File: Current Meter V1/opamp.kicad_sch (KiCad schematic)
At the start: 14 parts, among them U503 MCP6002-xSN

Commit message: microcontroller update
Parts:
- removed C506, C507: 100nF, symbol Device:C
- removed D501: BAT54A, Package_TO_SOT_SMD:SOT-23, symbol Diode:BAT54A
- removed D502: PRTR5V0U2X, Package_TO_SOT_SMD:SOT-143, symbol Power_Protection:PRTR5V0U2X
- removed R501, R503, R504, R505: 10k Ohms, symbol Device:R_US
- removed R502: 4.7k Ohms, symbol Device:R_US
- removed R506: 20k Ohms, symbol Device:R_US
- removed R507: 3.3K Ohms, symbol Device:R_US
- removed R508: 4.7K Ohms, symbol Device:R_US
- removed TP501: SMD Test Point, TestPoint:TestPoint_Keystone_5019_Miniature, symbol bfr_utilities:SMD_Test_Point
- removed U503: MCP6002-xSN, symbol Amplifier_Operational:MCP6002-xSN
- added C201, C202, C203: 100nF, symbol Device:C
- added D201, D203: BAT54A, Package_TO_SOT_SMD:SOT-23, symbol Diode:BAT54A
- added D202, D204: PRTR5V0U2X, Package_TO_SOT_SMD:SOT-143, symbol Power_Protection:PRTR5V0U2X
- added R201: 1.2k Ohms, symbol Device:R_US
- added R202, R203: 10k Ohms, symbol Device:R_US
- added R204, R207: 8.2K Ohms, symbol Device:R_US
- added R205: 24k Ohms, symbol Device:R_US
- added R206: 20k Ohms, symbol Device:R_US
- added R208: 22K Ohms, symbol Device:R_US
- added TP201, TP202: SMD Test Point, TestPoint:TestPoint_Keystone_5019_Miniature, symbol bfr_utilities:SMD_Test_Point
- added U201, U202: MCP6002-xSN, symbol Amplifier_Operational:MCP6002-xSN
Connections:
- net +3V3: now also D202.4 (VCC), D204.4 (VCC)
- net +5V: now also C202.1, D201.1, D203.1, R203.1, U201.8 (V+)
- net GND: now also C201.2, C202.2, C203.2, D202.1 (GND), D204.1 (GND), R201.2, R204.1, R208.2, U201.4 (V-), U201.5 (+)
- new net: R205.2, R206.1, U201.2 (-)
- new net: R207.1, TP202.1, U202.1, U202.2 (-)
- new net: R202.2, R205.1
- new net: U201.6 (-), U201.7
- new net 0.54V: C201.1, R201.1, R202.1, R203.2
- new net ADC: D202.2 (I/O1), R206.2, TP201.1, U201.1
- new net Sensor: D201.3, D203.3, R204.2, U201.3 (+), U202.3 (+)
- new net curr_sig: C203.1, D204.2 (I/O1), R207.2, R208.1
- no-connect marks 1 -> 4

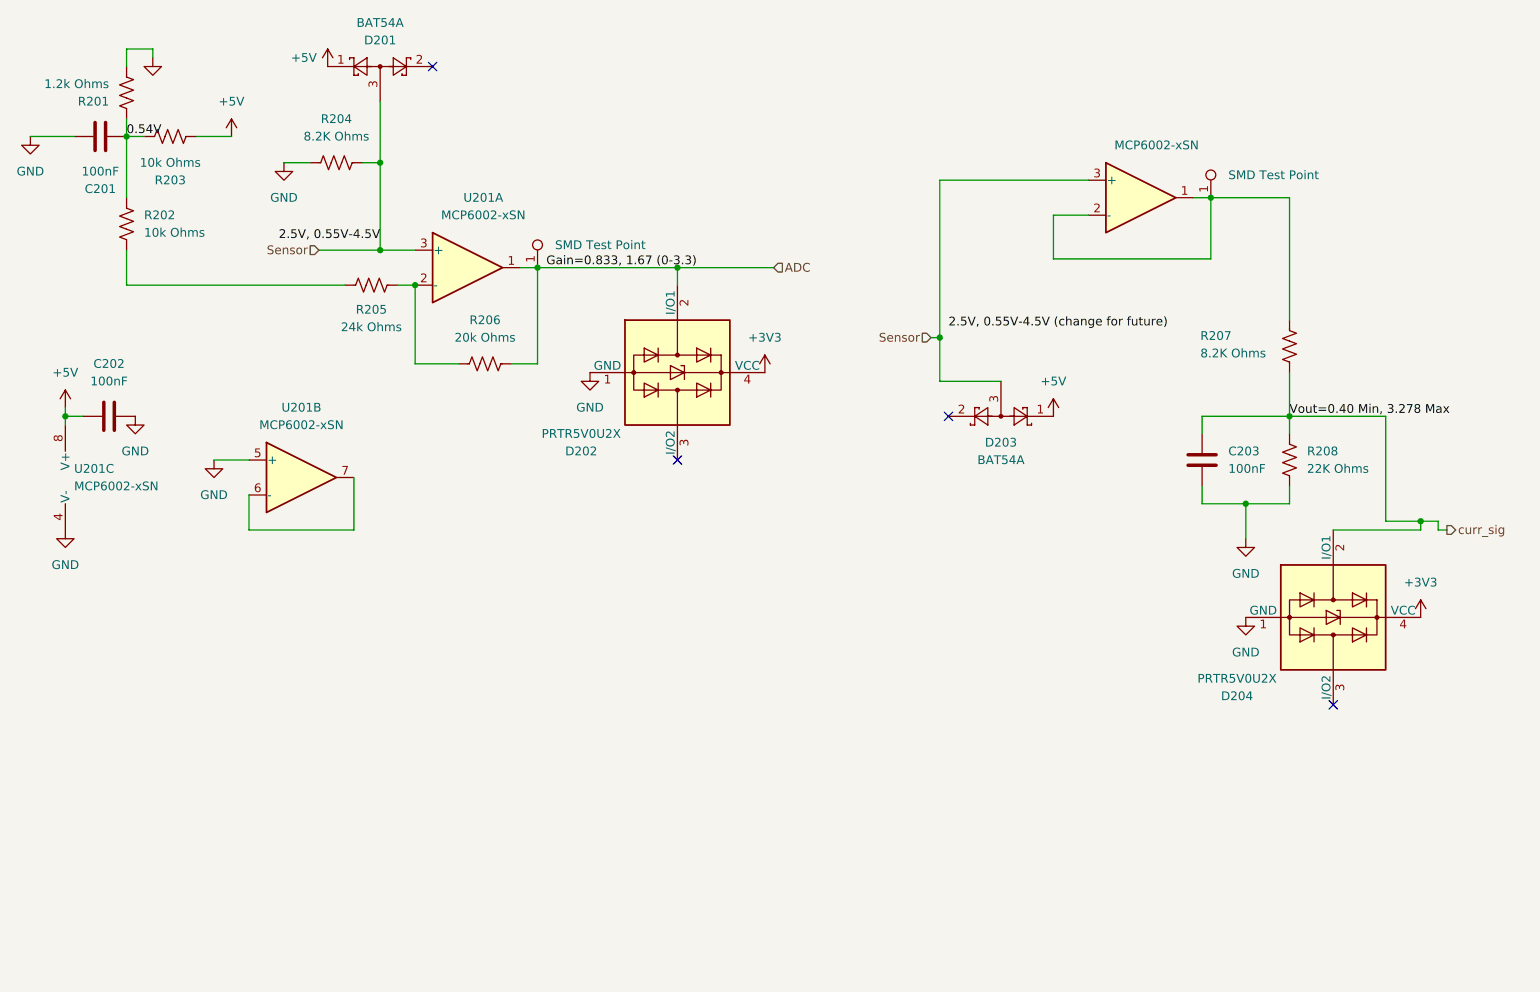
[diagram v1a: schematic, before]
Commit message: updated footprints
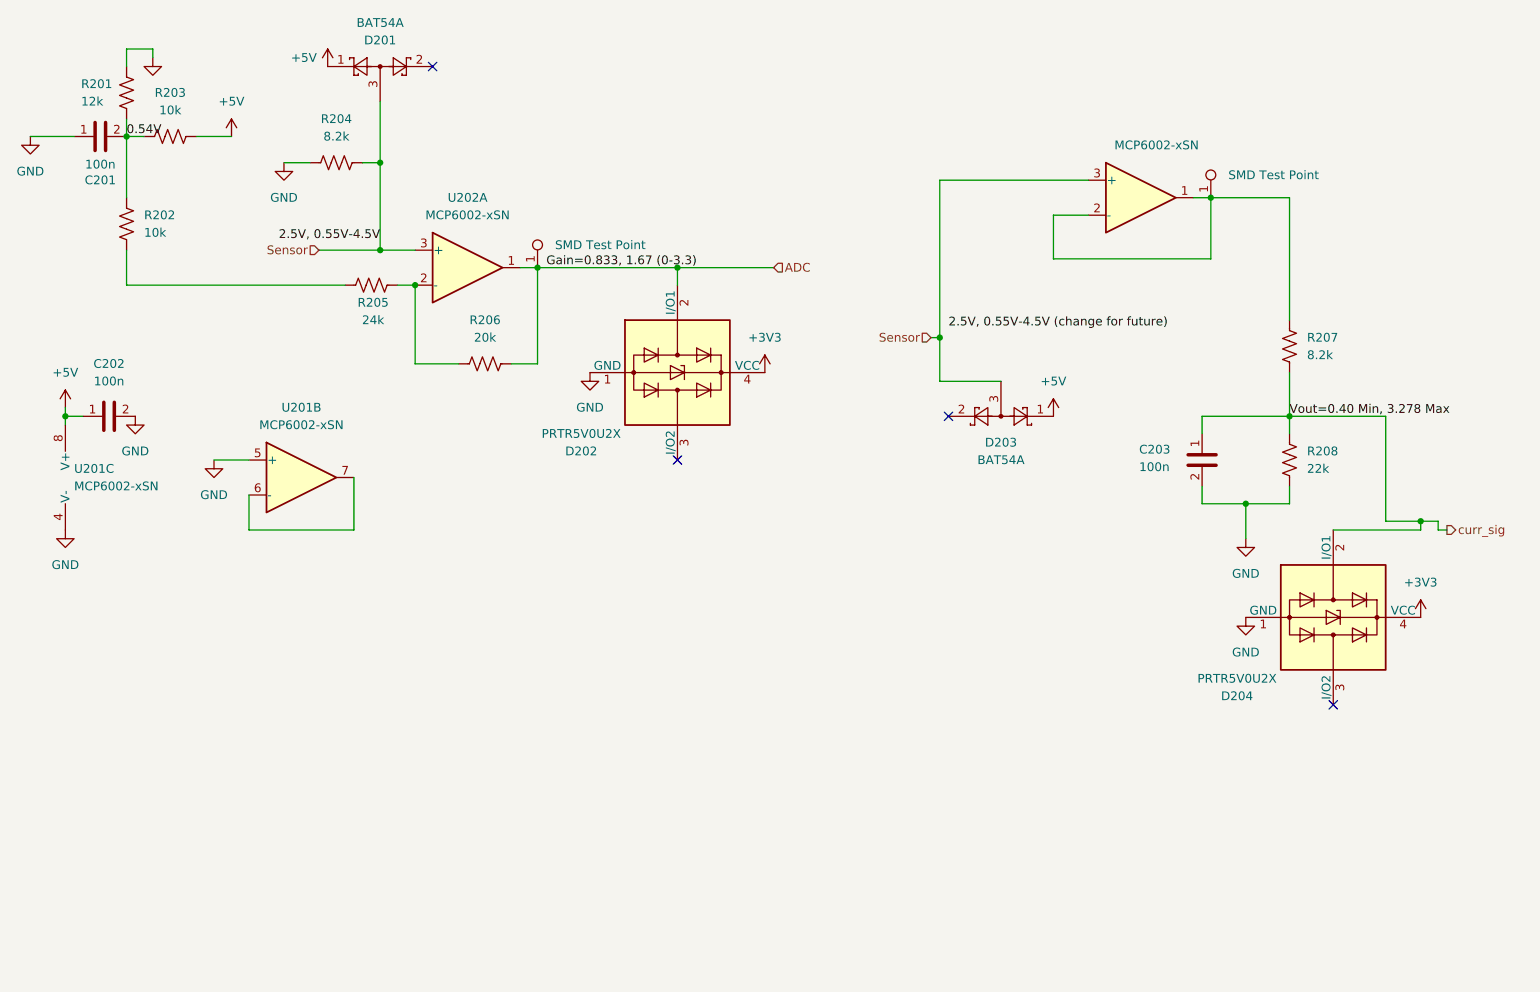
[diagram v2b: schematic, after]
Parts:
- removed C201, C202, C203: 100nF, symbol Device:C
- removed R201: 1.2k Ohms, symbol Device:R_US
- removed R202, R203: 10k Ohms, symbol Device:R_US
- removed R204, R207: 8.2K Ohms, symbol Device:R_US
- removed R205: 24k Ohms, symbol Device:R_US
- removed R206: 20k Ohms, symbol Device:R_US
- removed R208: 22K Ohms, symbol Device:R_US
- removed unit 1 of U201
- added C201, C202, C203: 100n, Capacitor_SMD:C_0805_2012Metric_Pad1.18x1.45mm_HandSolder, symbol bfr_capacitors:08051C104KAT4A
- added R201: 12k, Resistor_SMD:R_0805_2012Metric_Pad1.20x1.40mm_HandSolder, symbol bfr_resistors:RMCF0805FT12K0
- added R202, R203: 10k, Resistor_SMD:R_0805_2012Metric_Pad1.20x1.40mm_HandSolder, symbol bfr_resistors:RMCF0805FT10K0
- added R204, R207: 8.2k, Resistor_SMD:R_0805_2012Metric_Pad1.20x1.40mm_HandSolder, symbol bfr_resistors:RMCF0805FT8K20
- added R205: 24k, Resistor_SMD:R_0805_2012Metric_Pad1.20x1.40mm_HandSolder, symbol bfr_resistors:RMCF0805FT24K0
- added R206: 20k, Resistor_SMD:R_0805_2012Metric_Pad1.20x1.40mm_HandSolder, symbol bfr_resistors:RMCF0805FT20K0
- added R208: 22k, Resistor_SMD:R_0805_2012Metric_Pad1.20x1.40mm_HandSolder, symbol bfr_resistors:RMCF0805FT22K0
- added U202: MCP6002-xSN, Package_SO:SOIC-8_5.3x6.2mm_P1.27mm, symbol Amplifier_Operational:MCP6002-xSN
- renumbered U202 to U201
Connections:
- net +5V: now also C202.1, R203.2
- net 0.54V: now also C201.2, R201.2, R202.2, R203.1
- net ADC: now also R206.2, U202.1
- net GND: now also C201.1, C202.2, C203.2, R201.1, R204.1, R208.1
- net Sensor: now also R204.2, U202.3 (+)
- net curr_sig: now also C203.1, R207.1, R208.2
- net at TP202.1, U201.1, U201.2 (-): now also R207.2
- new net: R202.1, R205.1
- new net: R205.2, R206.1, U202.2 (-)

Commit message: footprints fully updated
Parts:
- U201: footprint (none) -> Package_SO:SOIC-8_5.3x6.2mm_P1.27mm
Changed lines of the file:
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@@
 			)
 		)
-		(property "Footprint" ""
+		(property "Footprint" "Package_SO:SOIC-8_5.3x6.2mm_P1.27mm"
 			(at 184.15 46.99 0)
 			(effects
@@
 			)
 		)
-		(property "Footprint" ""
+		(property "Footprint" "Package_SO:SOIC-8_5.3x6.2mm_P1.27mm"
 			(at 30.48 87.63 0)
 			(effects
@@
 			)
 		)
-		(property "Footprint" ""
+		(property "Footprint" "Package_SO:SOIC-8_5.3x6.2mm_P1.27mm"
 			(at 62.23 87.63 0)
 			(effects

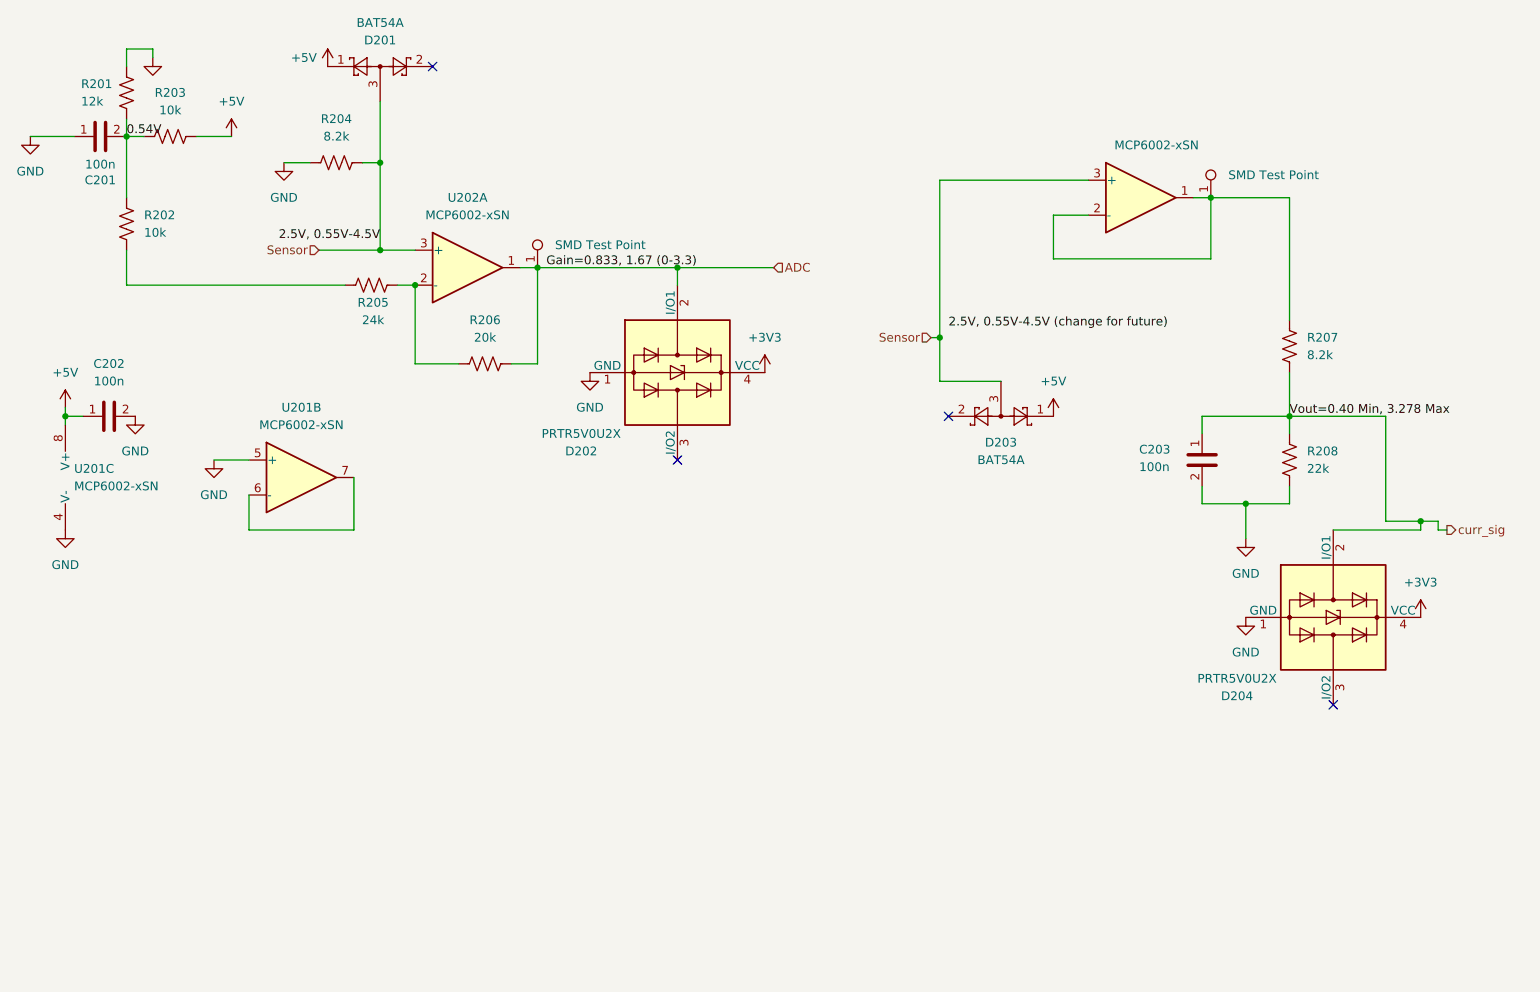
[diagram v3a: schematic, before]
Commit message: updates
started layout
deleted usb
fully updated op amp footprints
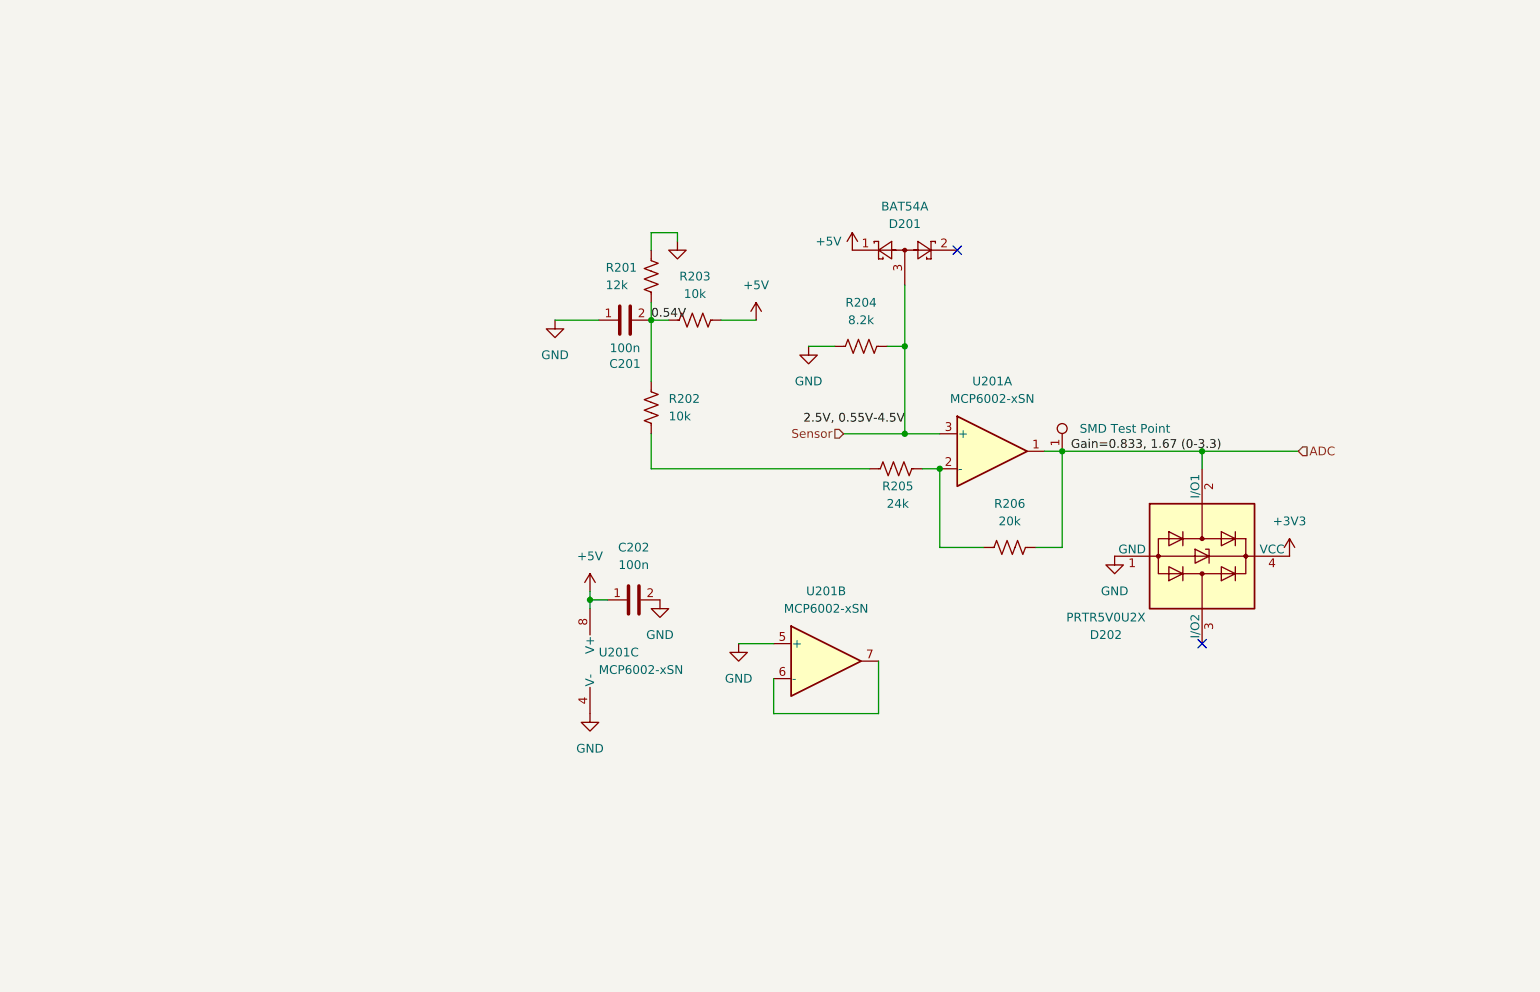
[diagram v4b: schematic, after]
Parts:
- removed C203: 100n, Capacitor_SMD:C_0805_2012Metric_Pad1.18x1.45mm_HandSolder, symbol bfr_capacitors:08051C104KAT4A
- removed D203: BAT54A, Package_TO_SOT_SMD:SOT-23, symbol Diode:BAT54A
- removed D204: PRTR5V0U2X, Package_TO_SOT_SMD:SOT-143, symbol Power_Protection:PRTR5V0U2X
- removed R207: 8.2k, Resistor_SMD:R_0805_2012Metric_Pad1.20x1.40mm_HandSolder, symbol bfr_resistors:RMCF0805FT8K20
- removed R208: 22k, Resistor_SMD:R_0805_2012Metric_Pad1.20x1.40mm_HandSolder, symbol bfr_resistors:RMCF0805FT22K0
- removed TP202: SMD Test Point, TestPoint:TestPoint_Keystone_5019_Miniature, symbol bfr_utilities:SMD_Test_Point
- removed U202: MCP6002-xSN, Package_SO:SOIC-8_5.3x6.2mm_P1.27mm, symbol Amplifier_Operational:MCP6002-xSN
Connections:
- net ADC: now also U201.1
- net at U201.2 (-): now also R205.2, R206.1; no longer U201.1
- no-connect marks 4 -> 2
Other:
- moved on the sheet: C201, C202, D201, D202, R201, R202, R203, R204, R205, R206

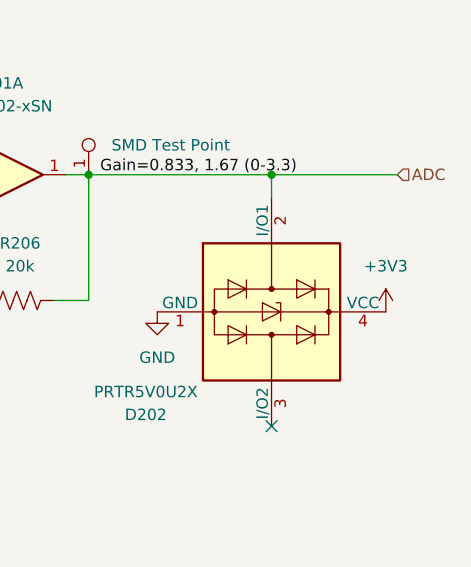
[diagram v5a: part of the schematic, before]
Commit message: changed everything to 5V
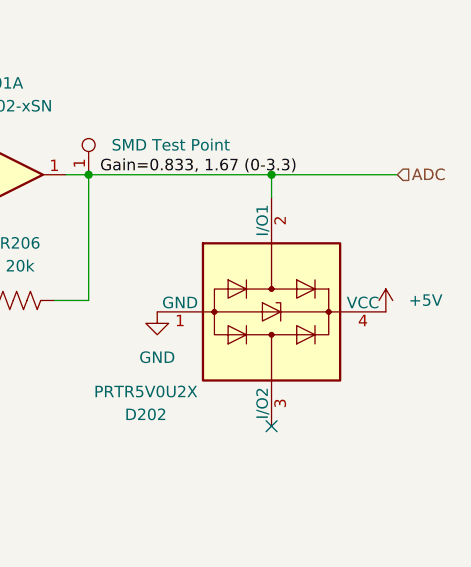
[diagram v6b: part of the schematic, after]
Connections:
- net +3V3 is gone; now on net +5V: D202.4 (VCC)
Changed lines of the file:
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@@
 			)
 		)
-		(property "Value" "+3V3"
-			(at 205.74 93.98 0)
+		(property "Value" "+5V"
+			(at 208.28 97.7899 0)
 			(effects
 				(font
 					(size 1.27 1.27)
 				)
+				(justify left)
 			)
 		)

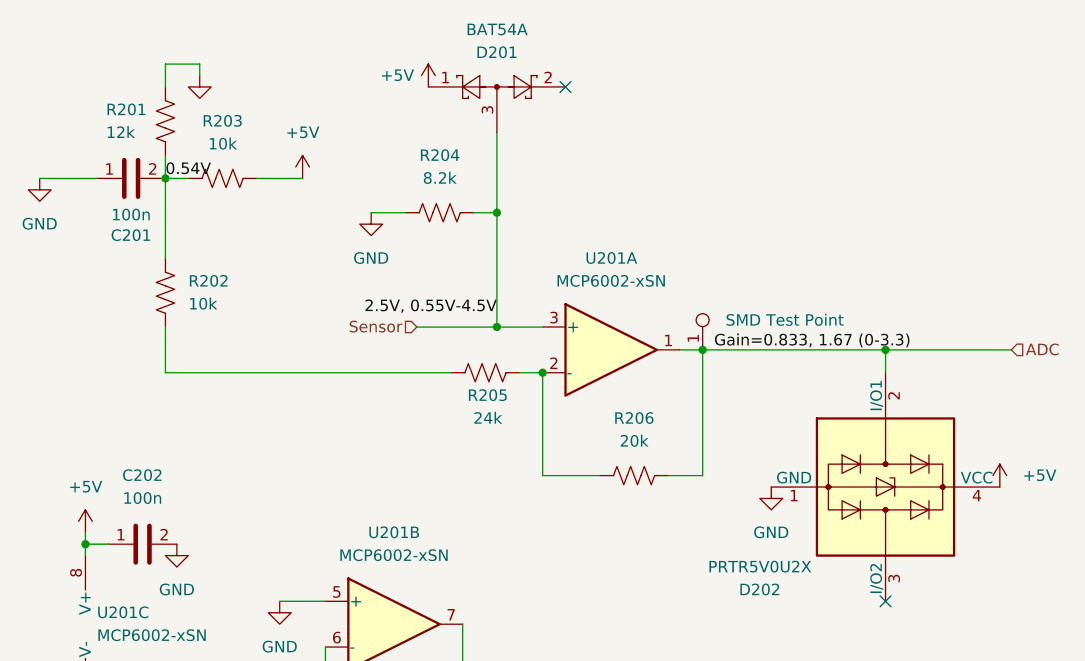
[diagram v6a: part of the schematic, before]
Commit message: updated layout
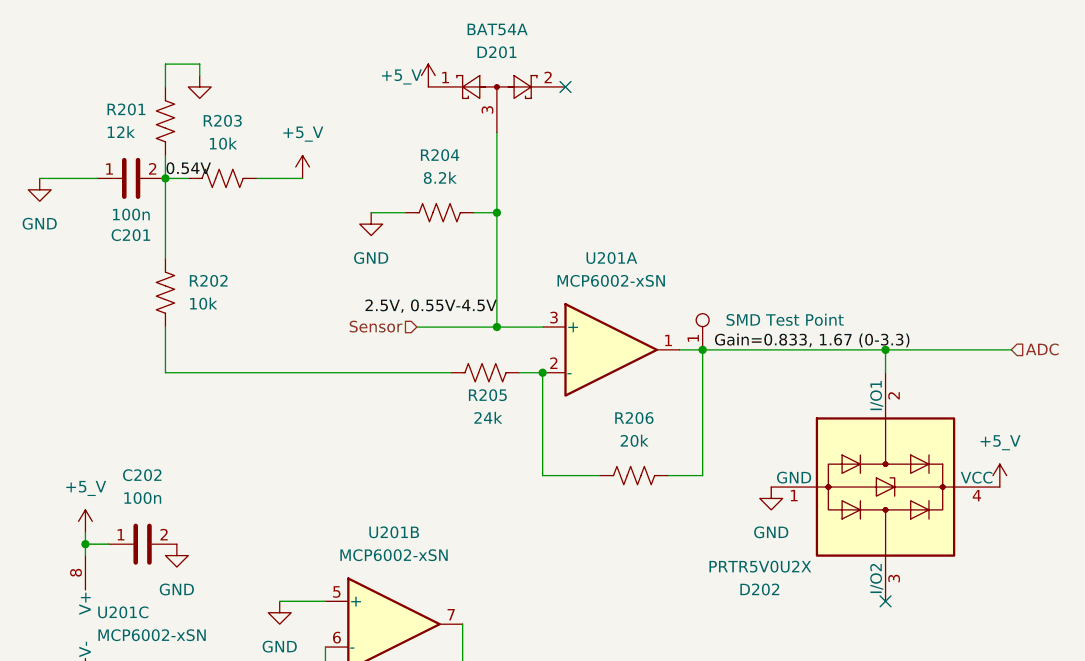
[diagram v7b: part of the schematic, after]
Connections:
- net +5V renamed +5_V
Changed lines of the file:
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@@
 			)
 		)
-		(property "Value" "+5V"
-			(at 208.28 97.7899 0)
-			(effects
-				(font
-					(size 1.27 1.27)
-				)
-				(justify left)
+		(property "Value" "+5_V"
+			(at 205.74 93.98 0)
+			(effects
+				(font
+					(size 1.27 1.27)
+				)
 			)
 		)
@@
 			)
 		)
-		(property "Value" "+5V"
+		(property "Value" "+5_V"
 			(at 128.27 59.69 0)
 			(effects
@@
 			)
 		)
-		(property "Value" "+5V"
+		(property "Value" "+5_V"
 			(at 104.14 99.06 0)
 			(effects
@@
 			)
 		)
-		(property "Value" "+5V"
+		(property "Value" "+5_V"
 			(at 136.906 53.34 0)
 			(effects
